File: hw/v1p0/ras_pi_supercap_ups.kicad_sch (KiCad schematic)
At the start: 63 parts, among them J1 Conn_01x03, J10 Barrel_Jack, J2 Conn_01x05, J3 Conn_01x03, J4 Force Power On, J5 171826-4, J6 LEDs and Buttons, J7 STLinkV2 Connector, Q1 IRF5305, SW1 Reset, U1 KA431SMFTF, U2 KA431SMFTF, U3 KA431SMFTF, U4 KA431SMFTF, U5 KA431SMFTF, U6 AMS1117-3.3, U7 STM8S003F3P

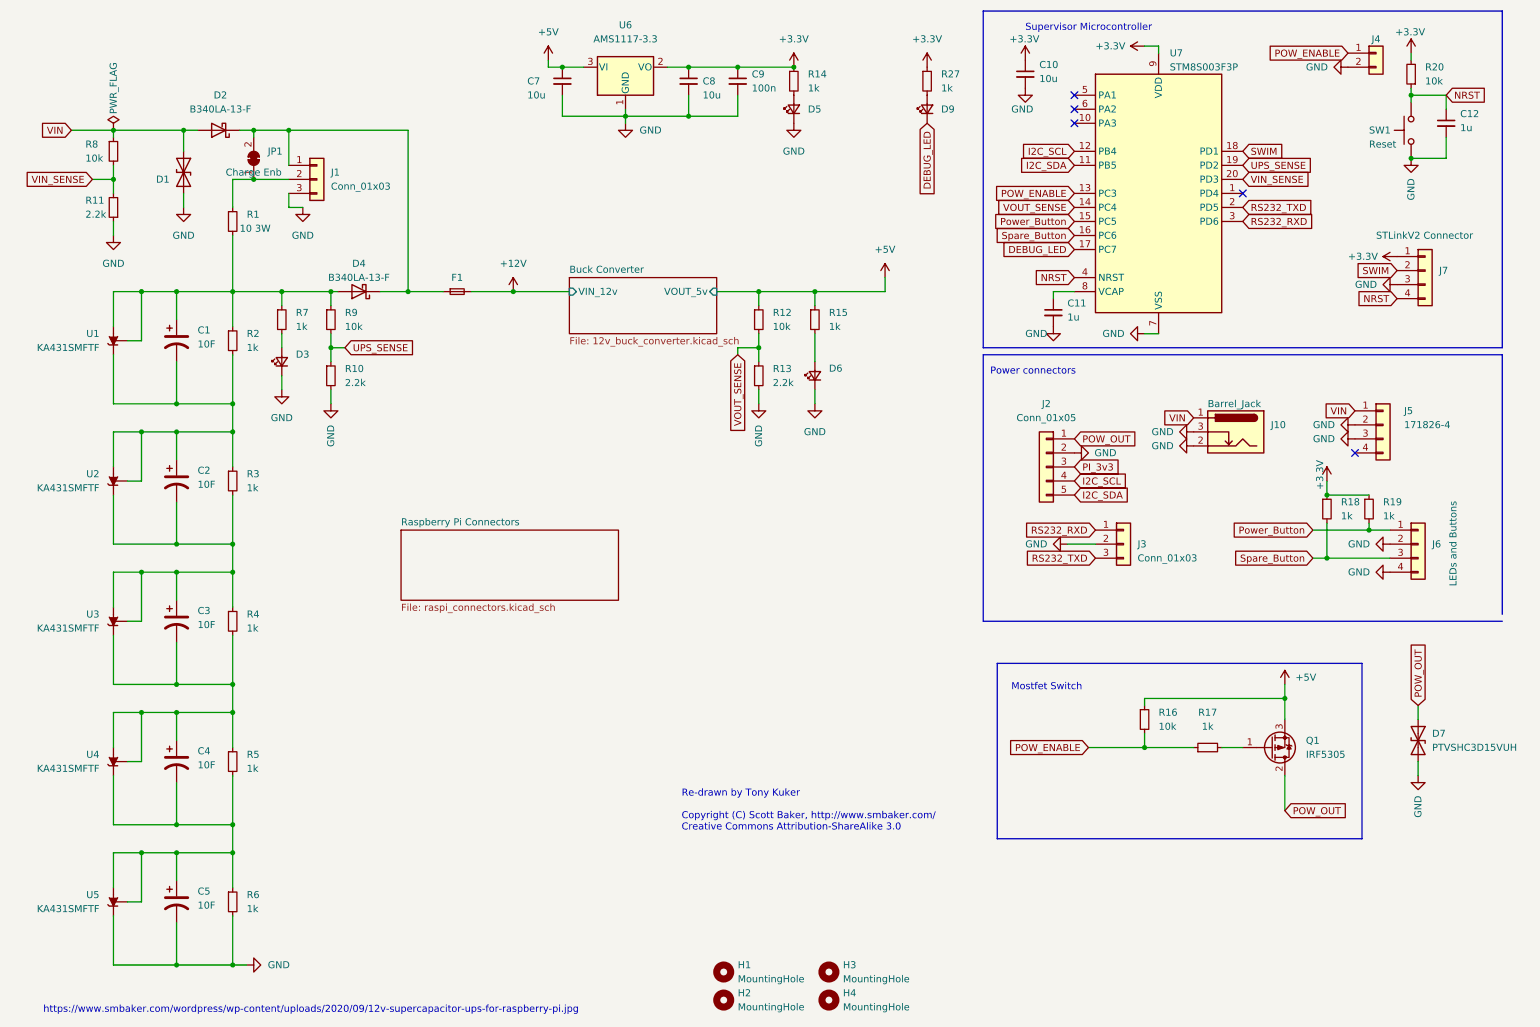
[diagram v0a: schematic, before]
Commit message: Last version before removing mosfet
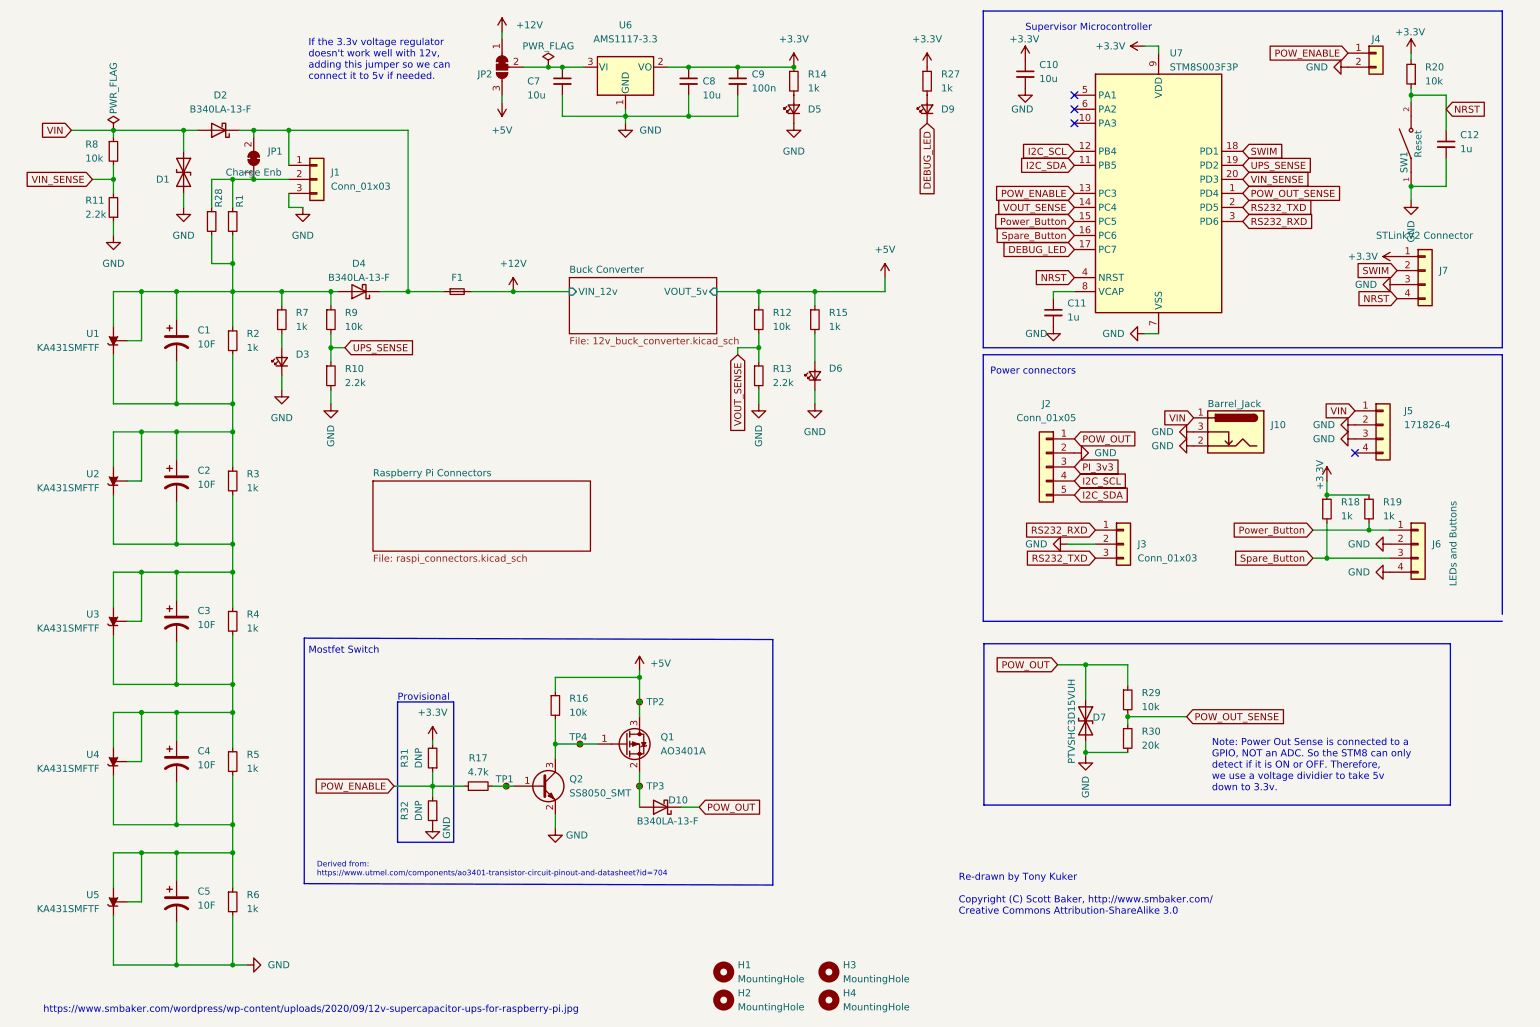
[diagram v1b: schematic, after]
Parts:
- removed Q1: IRF5305, Package_TO_SOT_SMD:TO-263-2, symbol Transistor_FET:SUD50P04-08
- added D10: B340LA-13-F, Diode_SMD:D_SMA, symbol Diode:1N5820
- added JP2: SolderJumper_3_Bridged12, Jumper:SolderJumper-3_P1.3mm_Bridged2Bar12_RoundedPad1.0x1.5mm_NumberLabels, symbol Jumper:SolderJumper_3_Bridged12
- added Q1: AO3401A, Package_TO_SOT_SMD:SOT-23, symbol Transistor_FET:AO3401A
- added Q2: SS8050_SMT, Package_TO_SOT_SMD:SOT-23, symbol supercap_library:SS8050_SMT
- added R28: 10 3W, raspberrypi_supercap_ups_lib:SMT_Resistor_4122, symbol Device:R_Small
- added R29: 10k, Resistor_SMD:R_0805_2012Metric, symbol Device:R_Small
- added R30: 20k, Resistor_SMD:R_0805_2012Metric, symbol Device:R_Small
- added R31, R32: DNP, Resistor_SMD:R_0805_2012Metric, symbol Device:R_Small
- added TP1, TP2, TP3, TP4: TestPoint_Small, TestPoint:TestPoint_Pad_D1.0mm, symbol Connector:TestPoint_Small
- C1, C2, C3, C4, C5: footprint Capacitor_THT:CP_Radial_D12.5mm_P5.00mm -> Capacitor_THT:CP_Radial_D10.0mm_P5.00mm
- D3, D5, D6, D9: LCSC C2293 -> C2297
- R1: footprint Resistor_THT:R_Axial_DIN0516_L15.5mm_D5.0mm_P25.40mm_Horizontal -> raspberrypi_supercap_ups_lib:SMT_Resistor_4122; LCSC DNP -> C306270
- R17: value 1k -> 4.7k; DigikeyPN CF14JT1K00CT-ND -> (none); LCSC C17513 -> C17673
- SW1: footprint Button_Switch_THT:SW_PUSH_6mm_H4.3mm -> SW_TS-1187A-B-A-B; symbol Switch:SW_Push -> TS-1187A-B-A-B:TS-1187A-B-A-B; LCSC DNP -> C318884; MANUFACTURER (none) -> XKB Industrial Precision; MAXIMUM_PACKAGE_HEIGHT (none) -> 1.5mm; PARTREV (none) -> A0; STANDARD (none) -> Manufacturer Recommendations
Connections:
- net +12V: now also JP2.1 (A)
- net +3V3: now also R31.2
- net +5V: now also JP2.3 (B), Q1.3 (D), TP2.1; no longer C7.1, U6.3 (VI)
- net GND: now also Q2.2 (Emitter), R30.2, R32.1
- net POW_ENABLE: now also R31.1, R32.2; no longer R16.2
- net POW_OUT: now also D10.1 (K), R29.1
- net at R17.2: now also Q2.1 (Base), TP1.1
- net at J1.2 (Pin_2), JP1.1 (A), R1.1: now also R28.1
- net at C1.1, D4.2 (A), R1.2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: now also R28.2
- net POW_OUT_SENSE: now reaches U7.1 (PD4)
- net POW_OUT_SENSE: now also R29.2, R30.1
- new net: C7.1, JP2.2 (C), U6.3 (VI)
- new net: D10.2 (A), Q1.2 (S), TP3.1
- new net: Q1.1 (G), Q2.3 (Collector), R16.2, TP4.1
- no-connect marks 5 -> 4
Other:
- note added: "Derived from: https://www.utmel.com/components/ao3401-transistor-circuit-pinout-and-datasheet?id=704"
- note added: "If the 3.3v voltage regulator doesn't work well with 12v, adding this jumper so we can connect it to 5v if needed."
- note added: "Note: Power Out Sense is connected to a GPIO, NOT an ADC. So the STM8 can only detect if it is ON or OFF. Therefore, we use a voltage dividier to take 5v down to 3.3v."
- note added: "Provisional"
- moved on the sheet: C12, D7, R16, R17

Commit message: Removed Mosfet - release candidate 1.0
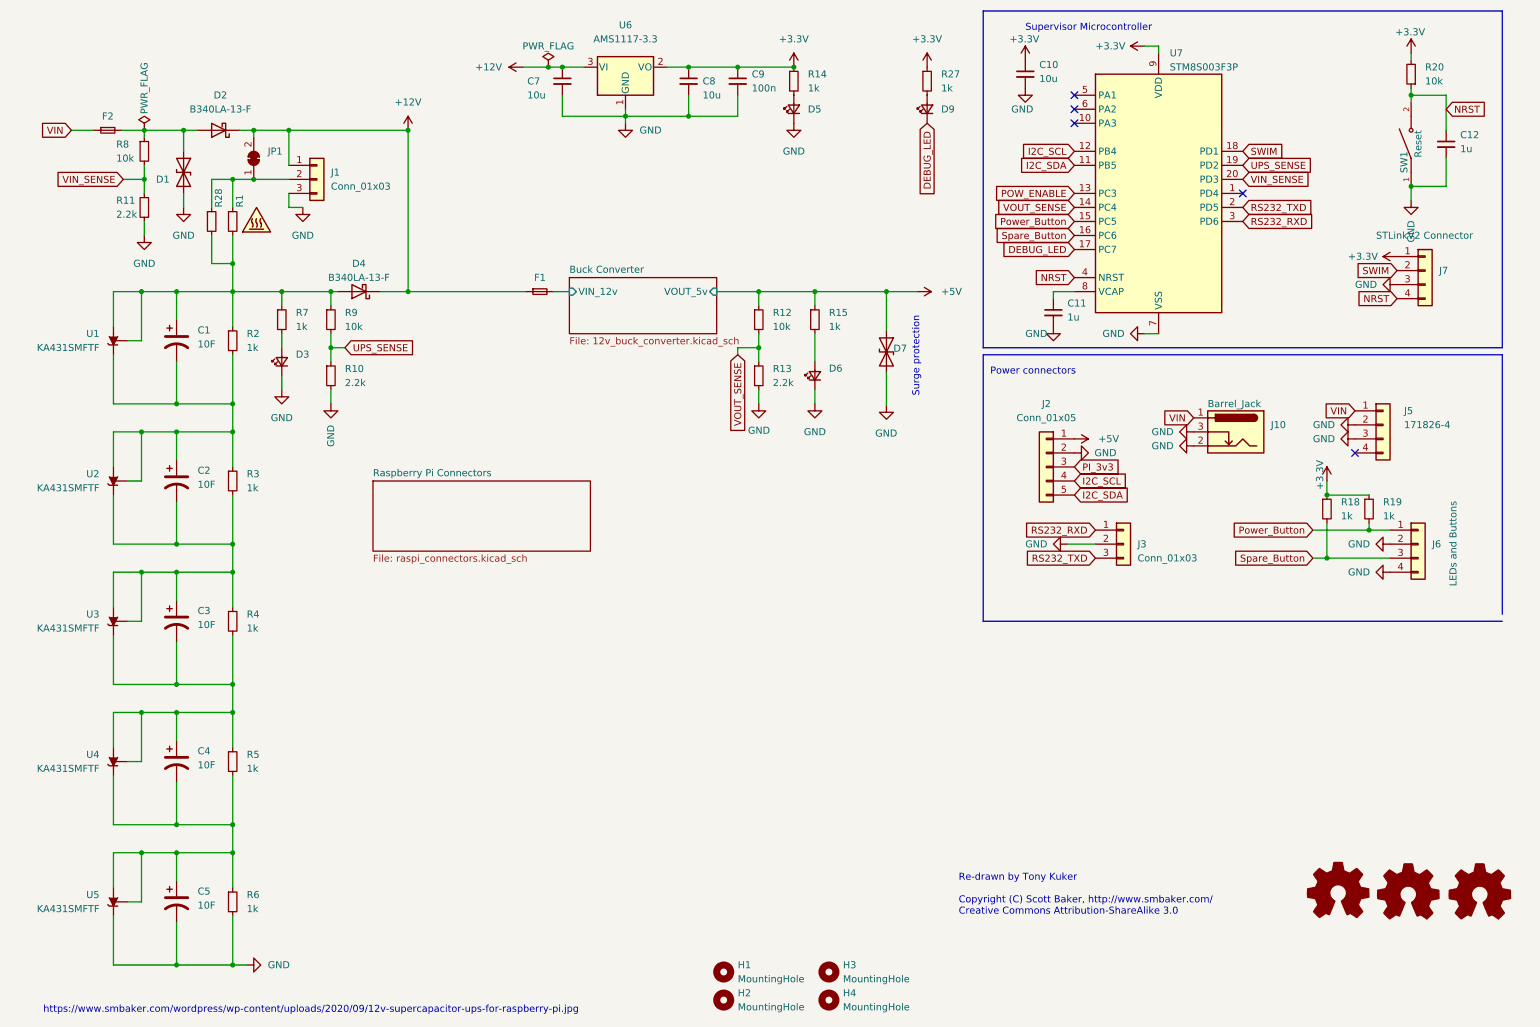
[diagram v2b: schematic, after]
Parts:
- removed D10: B340LA-13-F, Diode_SMD:D_SMA, symbol Diode:1N5820
- removed J4: Force Power On, Connector_PinHeader_2.54mm:PinHeader_1x02_P2.54mm_Vertical, symbol Connector_Generic:Conn_01x02
- removed JP2: SolderJumper_3_Bridged12, Jumper:SolderJumper-3_P1.3mm_Bridged2Bar12_RoundedPad1.0x1.5mm_NumberLabels, symbol Jumper:SolderJumper_3_Bridged12
- removed Q1: AO3401A, Package_TO_SOT_SMD:SOT-23, symbol Transistor_FET:AO3401A
- removed Q2: SS8050_SMT, Package_TO_SOT_SMD:SOT-23, symbol supercap_library:SS8050_SMT
- removed R16, R29: 10k, Resistor_SMD:R_0805_2012Metric, symbol Device:R_Small
- removed R17: 4.7k, Resistor_SMD:R_0805_2012Metric, symbol Device:R_Small
- removed R30: 20k, Resistor_SMD:R_0805_2012Metric, symbol Device:R_Small
- removed R31, R32: DNP, Resistor_SMD:R_0805_2012Metric, symbol Device:R_Small
- removed TP1, TP2, TP3, TP4: TestPoint_Small, TestPoint:TestPoint_Pad_D1.0mm, symbol Connector:TestPoint_Small
- added F2: Fuse_Small, Fuse:Fuse_1206_3216Metric, symbol Device:Fuse_Small
- added Z1: SYM_Hot_Small, raspberrypi_supercap_ups_lib:hot_warning_4, symbol Graphic:SYM_Hot_Small
- added Z2: Logo_Open_Hardware_Small, Symbol:CE-Logo_8.5x6mm_SilkScreen, symbol Graphic:Logo_Open_Hardware_Small
- added Z3: Logo_Open_Hardware_Small, Symbol:KiCad-Logo_5mm_Copper, symbol Graphic:Logo_Open_Hardware_Small
- added Z4: Logo_Open_Hardware_Small, Symbol:OSHW-Logo_7.5x8mm_SilkScreen, symbol Graphic:Logo_Open_Hardware_Small
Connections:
- net POW_OUT is gone; now on net +5V: D7.1 (A1), J2.1 (Pin_1)
- net +12V: now also C7.1, D2.1 (K), D4.1 (K), F1.1, J1.1 (Pin_1), JP1.2 (B), U6.3 (VI); no longer F1.2
- net VIN: now also F2.1; no longer D1.1 (A1), D2.2 (A), R8.1
- net POW_OUT_SENSE: no longer names the net of U7.1 (PD4)
- new net: D1.1 (A1), D2.2 (A), F2.2, R8.1
- new net Buck Converter/VIN_12v: F1.2
- no-connect marks 4 -> 5
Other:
- note added: "Surge protection"
- note removed: "Derived from: https://www.utmel.com/components/ao3401-transistor-circuit-pinout-and-datasheet?id=704"
- note removed: "If the 3.3v voltage regulator doesn't work well with 12v, adding this jumper so we can connect it to 5v if needed."
- note removed: "Mostfet Switch"
- note removed: "Note: Power Out Sense is connected to a GPIO, NOT an ADC. So the STM8 can only detect if it is ON or OFF. Therefore, we use a voltage dividier to take 5v down to 3.3v."
- note removed: "Provisional"
- moved on the sheet: D7, F1, R11, R8

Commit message: As-Ordered version
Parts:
- D2, D4: value B340LA-13-F -> SS54; LCSC C17101 -> C22452
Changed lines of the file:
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@@
     (in_bom yes) (on_board yes) (fields_autoplaced)
     (property "Reference" "D2" (id 0) (at 48.5775 29.21 0))
-    (property "Value" "B340LA-13-F" (id 1) (at 48.5775 31.75 0))
+    (property "Value" "SS54" (id 1) (at 48.5775 31.75 0))
     (property "Footprint" "Diode_SMD:D_SMA" (id 2) (at 48.26 31.115 0)
       (effects (font (size 1.27 1.27)) hide)
     )
-    (property "Datasheet" "https://datasheet.lcsc.com/lcsc/1809042014_Diodes-Incorporated-B340LA-13-F_C17101.pdf" (id 3) (at 48.26 35.56 0)
-      (effects (font (size 1.27 1.27)) hide)
-    )
-    (property "LCSC" "C17101" (id 4) (at 48.26 35.56 0)
+    (property "Datasheet" "https://datasheet.lcsc.com/lcsc/1810192041_MDD-Microdiode-Electronics--SS54_C22452.pdf" (id 3) (at 48.26 35.56 0)
+      (effects (font (size 1.27 1.27)) hide)
+    )
+    (property "LCSC" "C22452" (id 4) (at 48.26 35.56 0)
       (effects (font (size 1.27 1.27)) hide)
     )
@@
     (in_bom yes) (on_board yes)
     (property "Reference" "D4" (id 0) (at 73.66 59.69 0))
-    (property "Value" "B340LA-13-F" (id 1) (at 73.66 62.23 0))
+    (property "Value" "SS54" (id 1) (at 73.66 62.23 0))
     (property "Footprint" "Diode_SMD:D_SMA" (id 2) (at 73.66 60.325 0)
       (effects (font (size 1.27 1.27)) hide)
     )
-    (property "Datasheet" "https://datasheet.lcsc.com/lcsc/1809042014_Diodes-Incorporated-B340LA-13-F_C17101.pdf" (id 3) (at 73.66 64.77 0)
-      (effects (font (size 1.27 1.27)) hide)
-    )
-    (property "LCSC" "C17101" (id 4) (at 73.66 64.77 0)
+    (property "Datasheet" "https://datasheet.lcsc.com/lcsc/1810192041_MDD-Microdiode-Electronics--SS54_C22452.pdf" (id 3) (at 73.66 64.77 0)
+      (effects (font (size 1.27 1.27)) hide)
+    )
+    (property "LCSC" "C22452" (id 4) (at 73.66 64.77 0)
       (effects (font (size 1.27 1.27)) hide)
     )
@@
     )
     (path "/0d33a0a3-6701-41b8-8040-7340c4d8cd33"
-      (reference "D2") (unit 1) (value "B340LA-13-F") (footprint "Diode_SMD:D_SMA")
+      (reference "D2") (unit 1) (value "SS54") (footprint "Diode_SMD:D_SMA")
     )
     (path "/c1bd466d-fe29-493f-ab7a-15c6fc834f49"
@@
     )
     (path "/f35ed178-cd73-4dce-b724-5073a577c505"
-      (reference "D4") (unit 1) (value "B340LA-13-F") (footprint "Diode_SMD:D_SMA")
+      (reference "D4") (unit 1) (value "SS54") (footprint "Diode_SMD:D_SMA")
     )
     (path "/729ba23a-33ad-40f1-a0c2-8fe968618256"
@@
     )
     (path "/8f754e91-02e2-4214-a3e4-a044379db8a6/70f53d3a-f58b-46f3-aa80-cb222b643443"
-      (reference "D8") (unit 1) (value "B340A") (footprint "Diode_SMD:D_SMA")
+      (reference "D8") (unit 1) (value "SS54") (footprint "Diode_SMD:D_SMA")
     )
     (path "/da6c02eb-180c-4f37-8c54-5603905869f7"
